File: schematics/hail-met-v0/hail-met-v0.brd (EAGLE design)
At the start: 77.1 x 61 mm, 110 parts, among them IC1 MCP73871, J1 AVR_SPI_PRG_6PTH, U1 ATMEGA328P, Y1 16MHZ

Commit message: updated schematic with charge termination current resistor
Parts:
- R11: value 8K -> 100K
- RT2: value 80K -> 82K
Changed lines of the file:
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@@
 <attribute name="VALUE" x="2.794" y="40.513" size="0.4064" layer="27"/>
 </element>
-<element name="R11" library="SparkFun-Passives" package="0805" value="8K" x="67.6656" y="17.0942" smashed="yes" rot="R180">
+<element name="R11" library="SparkFun-Passives" package="0805" value="100K" x="67.6656" y="17.0942" smashed="yes" rot="R180">
 <attribute name="NAME" x="66.04" y="17.3609" size="0.4064" layer="25" rot="R180"/>
 <attribute name="VALUE" x="66.1162" y="16.8148" size="0.4064" layer="27" rot="R180"/>
@@
 <element name="RT1" library="SparkFun-Passives" package="0805" value="0" x="56.3626" y="21.5392" rot="R90"/>
 <element name="R13" library="SparkFun-Passives" package="0805" value="10K" x="48.8188" y="30.226" rot="R270"/>
-<element name="RT2" library="SparkFun-Passives" package="0805" value="80K" x="57.8612" y="23.368" rot="R270"/>
+<element name="RT2" library="SparkFun-Passives" package="0805" value="82K" x="57.8612" y="23.368" rot="R270"/>
 <element name="R16" library="SparkFun-Passives" package="0805" value="" x="3.81" y="35.56"/>
 <element name="R17" library="SparkFun-Passives" package="0805" value="" x="3.81" y="29.21"/>

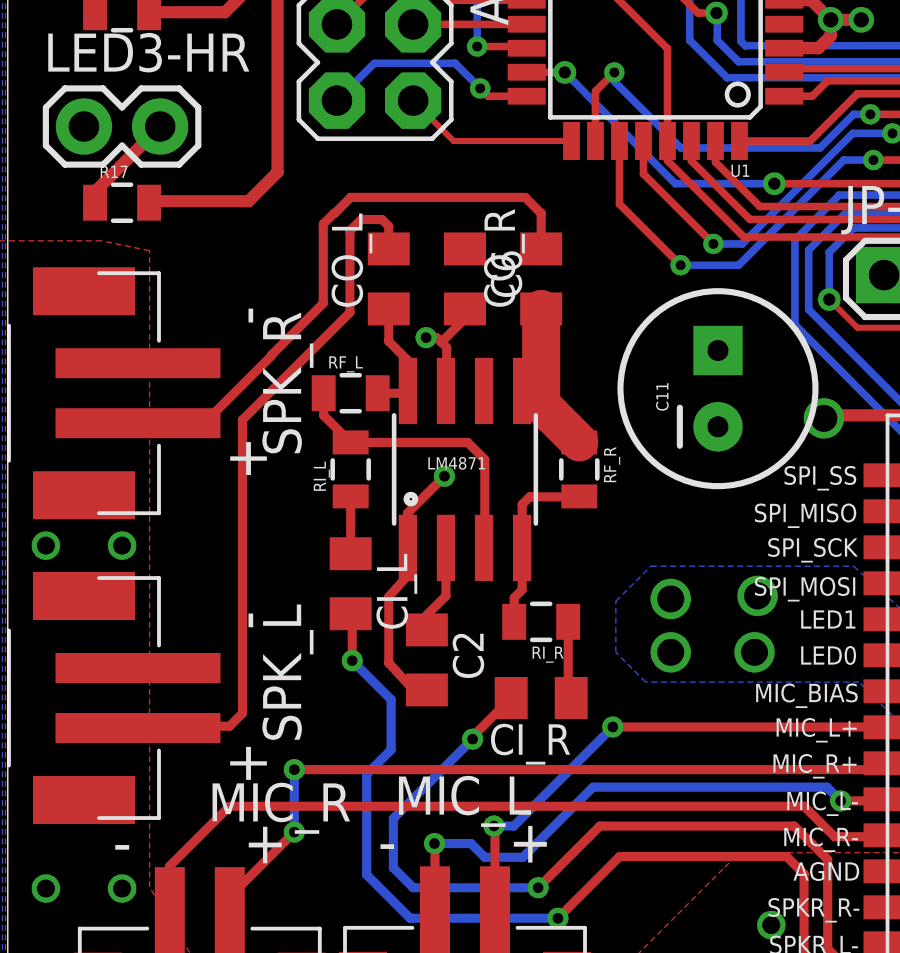
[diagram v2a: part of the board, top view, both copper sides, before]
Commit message: modified board with audio amp values
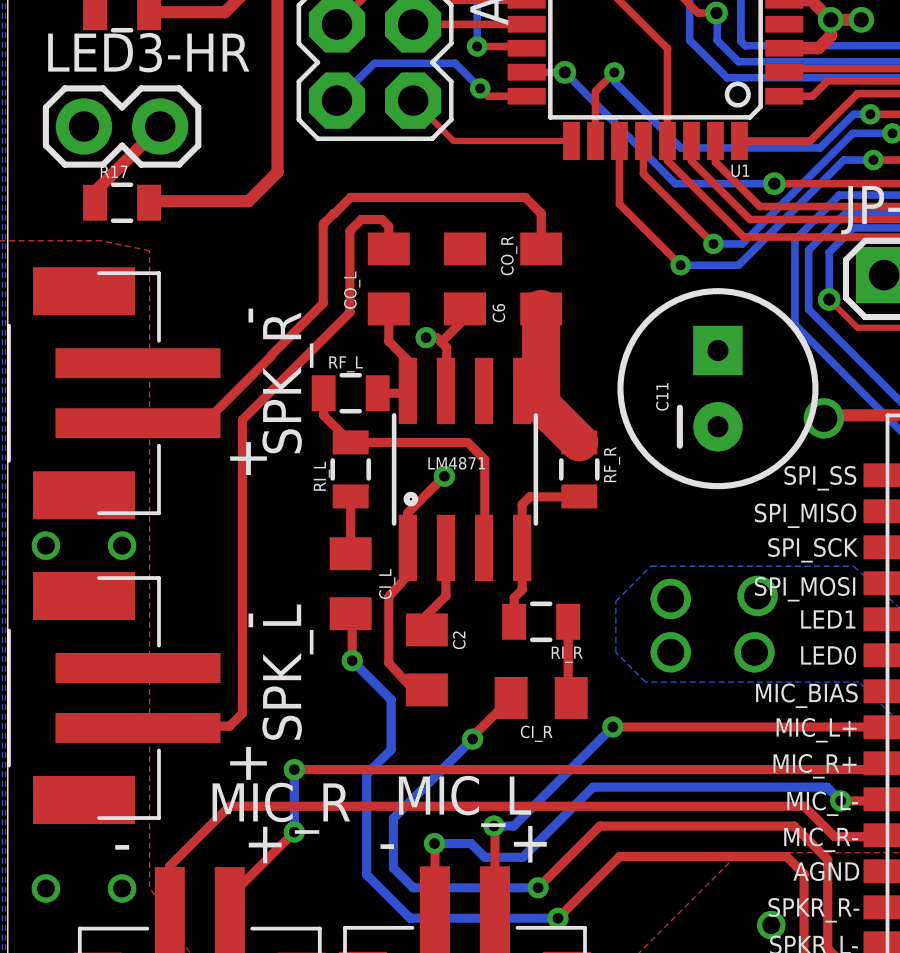
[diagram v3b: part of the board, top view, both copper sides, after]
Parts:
- C2: value 0.1uF -> 1uF
- CI_L, CI_R: value (none) -> 2.2uF (1uF)
- CO_L, CO_R: value (none) -> 100uF
- R1: value (none) -> 150
- R10, R16, R17, R19, R2, R20, R21: value (none) -> 6.8
- R14, R15, R24: value (none) -> 60
- R18, R22, R23: value (none) -> 40
- RF_L, RF_R: value 20k -> 180K (200K)
- RI_L, RI_R: value 20k -> 22K (20K)
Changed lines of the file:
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@@
 <attribute name="NAME" x="52.2986" y="32.3342" size="0.8128" layer="25" rot="R90"/>
 </element>
-<element name="R1" library="SparkFun-Passives" package="0805" value="" x="8.8646" y="50.8762" smashed="yes" rot="R270">
+<element name="R1" library="SparkFun-Passives" package="0805" value="150" x="8.8646" y="50.8762" smashed="yes" rot="R270">
 <attribute name="NAME" x="9.6901" y="51.6382" size="0.4064" layer="25" rot="R270"/>
 <attribute name="VALUE" x="7.4676" y="51.8922" size="0.4064" layer="27" rot="R270"/>
 </element>
-<element name="R10" library="SparkFun-Passives" package="0805" value="" x="3.81" y="41.91" smashed="yes">
+<element name="R10" library="SparkFun-Passives" package="0805" value="6.8" x="3.81" y="41.91" smashed="yes">
 <attribute name="NAME" x="3.048" y="42.7355" size="0.4064" layer="25"/>
 <attribute name="VALUE" x="2.794" y="40.513" size="0.4064" layer="27"/>
@@
 <element name="R13" library="SparkFun-Passives" package="0805" value="10K" x="48.8188" y="30.226" rot="R270"/>
 <element name="RT2" library="SparkFun-Passives" package="0805" value="82K" x="57.8612" y="23.368" rot="R270"/>
-<element name="R16" library="SparkFun-Passives" package="0805" value="" x="3.81" y="35.56"/>
-<element name="R17" library="SparkFun-Passives" package="0805" value="" x="3.81" y="29.21"/>
-<element name="R18" library="SparkFun-Passives" package="0805" value="" x="36.957" y="55.626" rot="R270"/>
-<element name="R19" library="SparkFun-Passives" package="0805" value="" x="30.5054" y="55.8038" rot="R270"/>
-<element name="R2" library="SparkFun-Passives" package="0805" value="" x="3.81" y="54.61"/>
-<element name="R20" library="SparkFun-Passives" package="0805" value="" x="24.2062" y="55.8038" rot="R270"/>
-<element name="R21" library="SparkFun-Passives" package="0805" value="" x="17.2466" y="55.8546" rot="R270"/>
-<element name="R22" library="SparkFun-Passives" package="0805" value="" x="3.81" y="48.26"/>
-<element name="R23" library="SparkFun-Passives" package="0805" value="" x="18.8722" y="55.8038" rot="R270"/>
+<element name="R16" library="SparkFun-Passives" package="0805" value="6.8" x="3.81" y="35.56"/>
+<element name="R17" library="SparkFun-Passives" package="0805" value="6.8" x="3.81" y="29.21"/>
+<element name="R18" library="SparkFun-Passives" package="0805" value="40" x="36.957" y="55.626" rot="R270"/>
+<element name="R19" library="SparkFun-Passives" package="0805" value="6.8" x="30.5054" y="55.8038" rot="R270"/>
+<element name="R2" library="SparkFun-Passives" package="0805" value="6.8" x="3.81" y="54.61"/>
+<element name="R20" library="SparkFun-Passives" package="0805" value="6.8" x="24.2062" y="55.8038" rot="R270"/>
+<element name="R21" library="SparkFun-Passives" package="0805" value="6.8" x="17.2466" y="55.8546" rot="R270"/>
+<element name="R22" library="SparkFun-Passives" package="0805" value="40" x="3.81" y="48.26"/>
+<element name="R23" library="SparkFun-Passives" package="0805" value="40" x="18.8722" y="55.8038" rot="R270"/>
 <element name="R3" library="SparkFun-Passives" package="0805" value="270K" x="57.785" y="17.0688"/>
 <element name="R4" library="SparkFun-Passives" package="0805" value="100K" x="56.0578" y="18.9484"/>
@@
 </element>
 <element name="LM4871" library="SparkFun" package="SO08" value="LM4871" x="15.24" y="20.32"/>
-<element name="RI_L" library="SparkFun-Passives" package="0805" value="20k" x="11.43" y="20.32" rot="R90"/>
-<element name="C2" library="adafruit" package="C0805K" value="0.1uF" x="13.97" y="13.97" rot="R270"/>
-<element name="RI_R" library="SparkFun-Passives" package="0805" value="20k" x="17.78" y="15.24" rot="R180"/>
-<element name="C6" library="adafruit" package="C0805K" value="0.1uF" x="15.24" y="26.67" rot="R270"/>
-<element name="RF_R" library="SparkFun-Passives" package="0805" value="20k" x="19.05" y="20.32" rot="R270"/>
-<element name="RF_L" library="SparkFun-Passives" package="0805" value="20k" x="11.43" y="22.86"/>
-<element name="CI_L" library="adafruit" package="C0805K" value="" x="11.43" y="16.51" rot="R270"/>
-<element name="CI_R" library="adafruit" package="C0805K" value="" x="17.78" y="12.7" rot="R180"/>
+<element name="RI_L" library="SparkFun-Passives" package="0805" value="22K (20K)" x="11.43" y="20.32" rot="R90"/>
+<element name="C2" library="adafruit" package="C0805K" value="1uF" x="13.97" y="13.97" smashed="yes" rot="R270">
+<attribute name="NAME" x="14.845" y="14.97" size="0.4064" layer="25" rot="R270"/>
+<attribute name="VALUE" x="12.5526" y="13.4206" size="0.4064" layer="27" rot="R270"/>
+</element>
+<element name="RI_R" library="SparkFun-Passives" package="0805" value="22K (20K)" x="17.78" y="15.24" smashed="yes" rot="R180">
+<attribute name="NAME" x="19.177" y="14.4145" size="0.4064" layer="25" rot="R180"/>
+<attribute name="VALUE" x="18.796" y="16.637" size="0.4064" layer="27" rot="R180"/>
+</element>
+<element name="C6" library="adafruit" package="C0805K" value="0.1uF" x="15.24" y="26.67" smashed="yes" rot="R270">
+<attribute name="NAME" x="16.1658" y="25.8666" size="0.4064" layer="25" rot="R270"/>
+<attribute name="VALUE" x="13.975" y="27.1366" size="0.4064" layer="27" rot="R270"/>
+</element>
+<element name="RF_R" library="SparkFun-Passives" package="0805" value="180K (200K)" x="19.05" y="20.32" rot="R270"/>
+<element name="RF_L" library="SparkFun-Passives" package="0805" value="180K (200K)" x="11.43" y="22.86"/>
+<element name="CI_L" library="adafruit" package="C0805K" value="2.2uF (1uF)" x="11.43" y="16.51" smashed="yes" rot="R270">
+<attribute name="NAME" x="12.3812" y="17.002" size="0.4064" layer="25" rot="R270"/>
+<attribute name="VALUE" x="10.165" y="17.5354" size="0.4064" layer="27" rot="R270"/>
+</element>
+<element name="CI_R" library="adafruit" package="C0805K" value="2.2uF (1uF)" x="17.78" y="12.7" smashed="yes" rot="R180">
+<attribute name="NAME" x="18.1704" y="11.7742" size="0.4064" layer="25" rot="R180"/>
+<attribute name="VALUE" x="17.764" y="13.9142" size="0.4064" layer="27" rot="R180"/>
+</element>
 <element name="NTC_THERM" library="SparkFun-Connectors" package="1X02" value="M02PTH" x="54.1274" y="25.4" smashed="yes" rot="R180">
 <attribute name="NAME" x="57.4802" y="24.384" size="0.8128" layer="25" ratio="10" rot="R180"/>
 </element>
 <element name="MPU-6050" library="SparkFun-Connectors" package="1X08_LOCK" value="" x="48.26" y="57.15"/>
-<element name="CO_L" library="adafruit" package="C0805K" value="" x="12.7" y="26.67" rot="R90"/>
-<element name="CO_R" library="adafruit" package="C0805K" value="" x="17.78" y="26.67" rot="R90"/>
+<element name="CO_L" library="adafruit" package="C0805K" value="100uF" x="12.7" y="26.67" smashed="yes" rot="R90">
+<attribute name="NAME" x="11.6218" y="25.6446" size="0.4064" layer="25" rot="R90"/>
+<attribute name="VALUE" x="11.7298" y="27.5242" size="0.4064" layer="27" rot="R90"/>
+</element>
+<element name="CO_R" library="adafruit" package="C0805K" value="100uF" x="17.78" y="26.67" smashed="yes" rot="R90">
+<attribute name="NAME" x="16.8542" y="26.7622" size="0.4064" layer="25" rot="R90"/>
+<attribute name="VALUE" x="19.1466" y="26.559" size="0.4064" layer="27" rot="R90"/>
+</element>
 <element name="PWR_BUTTON" library="SparkFun-Connectors" package="1X02" value="M02PTH" x="64.8208" y="12.0904" smashed="yes" rot="R270">
 <attribute name="NAME" x="66.1162" y="14.6812" size="0.8128" layer="25" ratio="10" rot="R270"/>
@@
 <attribute name="NAME" x="55.3212" y="46.9138" size="1.27" layer="25" ratio="10" rot="R90"/>
 </element>
-<element name="R14" library="SparkFun-Passives" package="0805" value="" x="57.15" y="53.975" rot="R90"/>
+<element name="R14" library="SparkFun-Passives" package="0805" value="60" x="57.15" y="53.975" rot="R90"/>
 <element name="LED_LB" library="SparkFun-Connectors" package="1X02" value="M02PTH" x="62.23" y="48.26" smashed="yes" rot="R90">
 <attribute name="NAME" x="60.4012" y="46.9138" size="1.27" layer="25" ratio="10" rot="R90"/>
 </element>
-<element name="R15" library="SparkFun-Passives" package="0805" value="" x="62.23" y="53.975" rot="R90"/>
+<element name="R15" library="SparkFun-Passives" package="0805" value="60" x="62.23" y="53.975" rot="R90"/>
 <element name="LED_CHG" library="SparkFun-Connectors" package="1X02" value="M02PTH" x="67.31" y="48.26" smashed="yes" rot="R90">
 <attribute name="NAME" x="65.4812" y="46.9138" size="1.27" layer="25" ratio="10" rot="R90"/>
 </element>
-<element name="R24" library="SparkFun-Passives" package="0805" value="" x="67.31" y="53.975" rot="R90"/>
+<element name="R24" library="SparkFun-Passives" package="0805" value="60" x="67.31" y="53.975" rot="R90"/>
 <element name="JP-BT3" library="SparkFun-Connectors" package="1X04_LOCK" value="" x="69.85" y="27.94" rot="R90"/>
 <element name="AT_PINS" library="SparkFun-Connectors" package="2X4" value="M04X2" x="12.2428" y="36.4236" rot="R270"/>

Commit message: updated schematic with new LED driver values
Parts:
- R10, R16, R17, R19, R2, R20, R21: value 6.8 -> 8.2
- R18, R22, R23: value 40 -> 43
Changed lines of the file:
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@@
 <?xml version="1.0" encoding="utf-8"?>
 <!DOCTYPE eagle SYSTEM "eagle.dtd">
-<eagle version="7.1.0">
+<eagle version="7.2.0">
 <drawing>
 <settings>
@@
 <attribute name="VALUE" x="7.4676" y="51.8922" size="0.4064" layer="27" rot="R270"/>
 </element>
-<element name="R10" library="SparkFun-Passives" package="0805" value="6.8" x="3.81" y="41.91" smashed="yes">
+<element name="R10" library="SparkFun-Passives" package="0805" value="8.2" x="3.81" y="41.91" smashed="yes">
 <attribute name="NAME" x="3.048" y="42.7355" size="0.4064" layer="25"/>
 <attribute name="VALUE" x="2.794" y="40.513" size="0.4064" layer="27"/>
@@
 <element name="R13" library="SparkFun-Passives" package="0805" value="10K" x="48.8188" y="30.226" rot="R270"/>
 <element name="RT2" library="SparkFun-Passives" package="0805" value="82K" x="57.8612" y="23.368" rot="R270"/>
-<element name="R16" library="SparkFun-Passives" package="0805" value="6.8" x="3.81" y="35.56"/>
-<element name="R17" library="SparkFun-Passives" package="0805" value="6.8" x="3.81" y="29.21"/>
-<element name="R18" library="SparkFun-Passives" package="0805" value="40" x="36.957" y="55.626" rot="R270"/>
-<element name="R19" library="SparkFun-Passives" package="0805" value="6.8" x="30.5054" y="55.8038" rot="R270"/>
-<element name="R2" library="SparkFun-Passives" package="0805" value="6.8" x="3.81" y="54.61"/>
-<element name="R20" library="SparkFun-Passives" package="0805" value="6.8" x="24.2062" y="55.8038" rot="R270"/>
-<element name="R21" library="SparkFun-Passives" package="0805" value="6.8" x="17.2466" y="55.8546" rot="R270"/>
-<element name="R22" library="SparkFun-Passives" package="0805" value="40" x="3.81" y="48.26"/>
-<element name="R23" library="SparkFun-Passives" package="0805" value="40" x="18.8722" y="55.8038" rot="R270"/>
+<element name="R16" library="SparkFun-Passives" package="0805" value="8.2" x="3.81" y="35.56"/>
+<element name="R17" library="SparkFun-Passives" package="0805" value="8.2" x="3.81" y="29.21"/>
+<element name="R18" library="SparkFun-Passives" package="0805" value="43" x="36.957" y="55.626" rot="R270"/>
+<element name="R19" library="SparkFun-Passives" package="0805" value="8.2" x="30.5054" y="55.8038" rot="R270"/>
+<element name="R2" library="SparkFun-Passives" package="0805" value="8.2" x="3.81" y="54.61"/>
+<element name="R20" library="SparkFun-Passives" package="0805" value="8.2" x="24.2062" y="55.8038" rot="R270"/>
+<element name="R21" library="SparkFun-Passives" package="0805" value="8.2" x="17.2466" y="55.8546" rot="R270"/>
+<element name="R22" library="SparkFun-Passives" package="0805" value="43" x="3.81" y="48.26"/>
+<element name="R23" library="SparkFun-Passives" package="0805" value="43" x="18.8722" y="55.8038" rot="R270"/>
 <element name="R3" library="SparkFun-Passives" package="0805" value="270K" x="57.785" y="17.0688"/>
 <element name="R4" library="SparkFun-Passives" package="0805" value="100K" x="56.0578" y="18.9484"/>
